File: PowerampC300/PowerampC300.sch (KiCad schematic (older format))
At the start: 101 parts, among them J1 Conn_01x02, J2 Conn_01x02, J3 Conn_01x02, J4 Conn_01x01, J5 Conn_01x01, J6 Conn_01x01, J7 Conn_01x01, J8 Conn_01x02, J9 Conn_Coaxial, Q1 BC546, Q10 MJE350, Q11 MJE340, Q12 MJE340, Q13 BC546, Q14 BC556, Q15 MJE340, Q16 MJE350, Q17 MJL3281A, Q18 MJL1302A, Q19 MJL3281A, Q2 BC546, Q20 MJL1302A, Q21 MJL3281A, Q22 MJL1302A, Q23 MJL3281A, Q24 MJL1302A, Q3 BC556, Q4 BC556, Q5 BC546, Q6 BC546, Q7 BC546, Q8 MPSA92, Q9 BC556

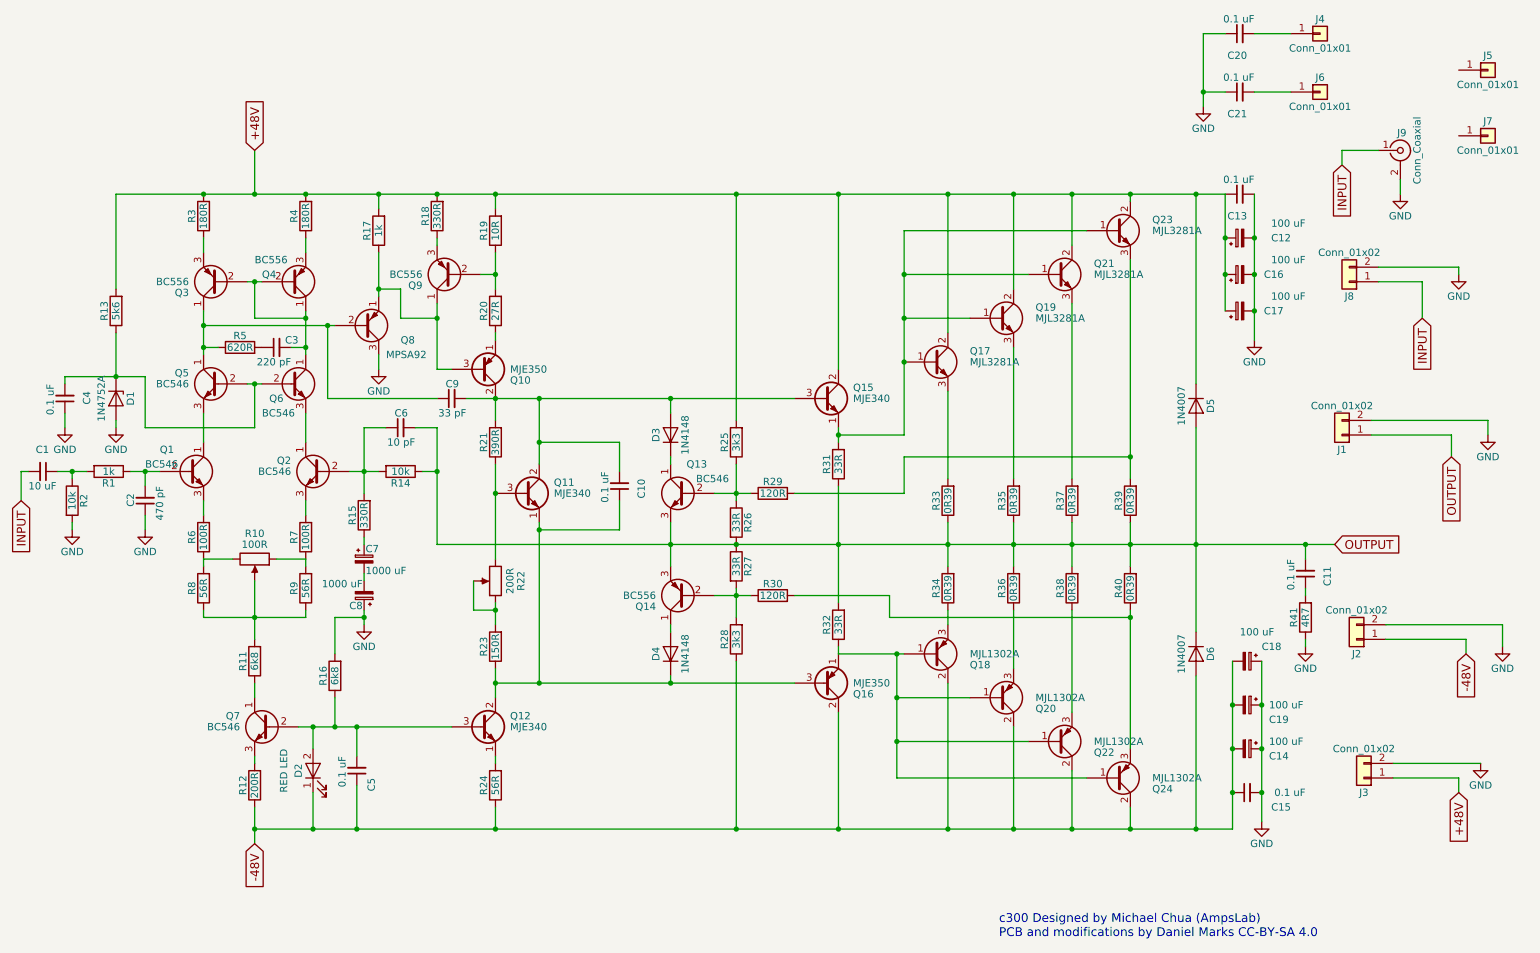
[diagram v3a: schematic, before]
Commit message: Changed softstart and Poweramp to TO-220 transistors
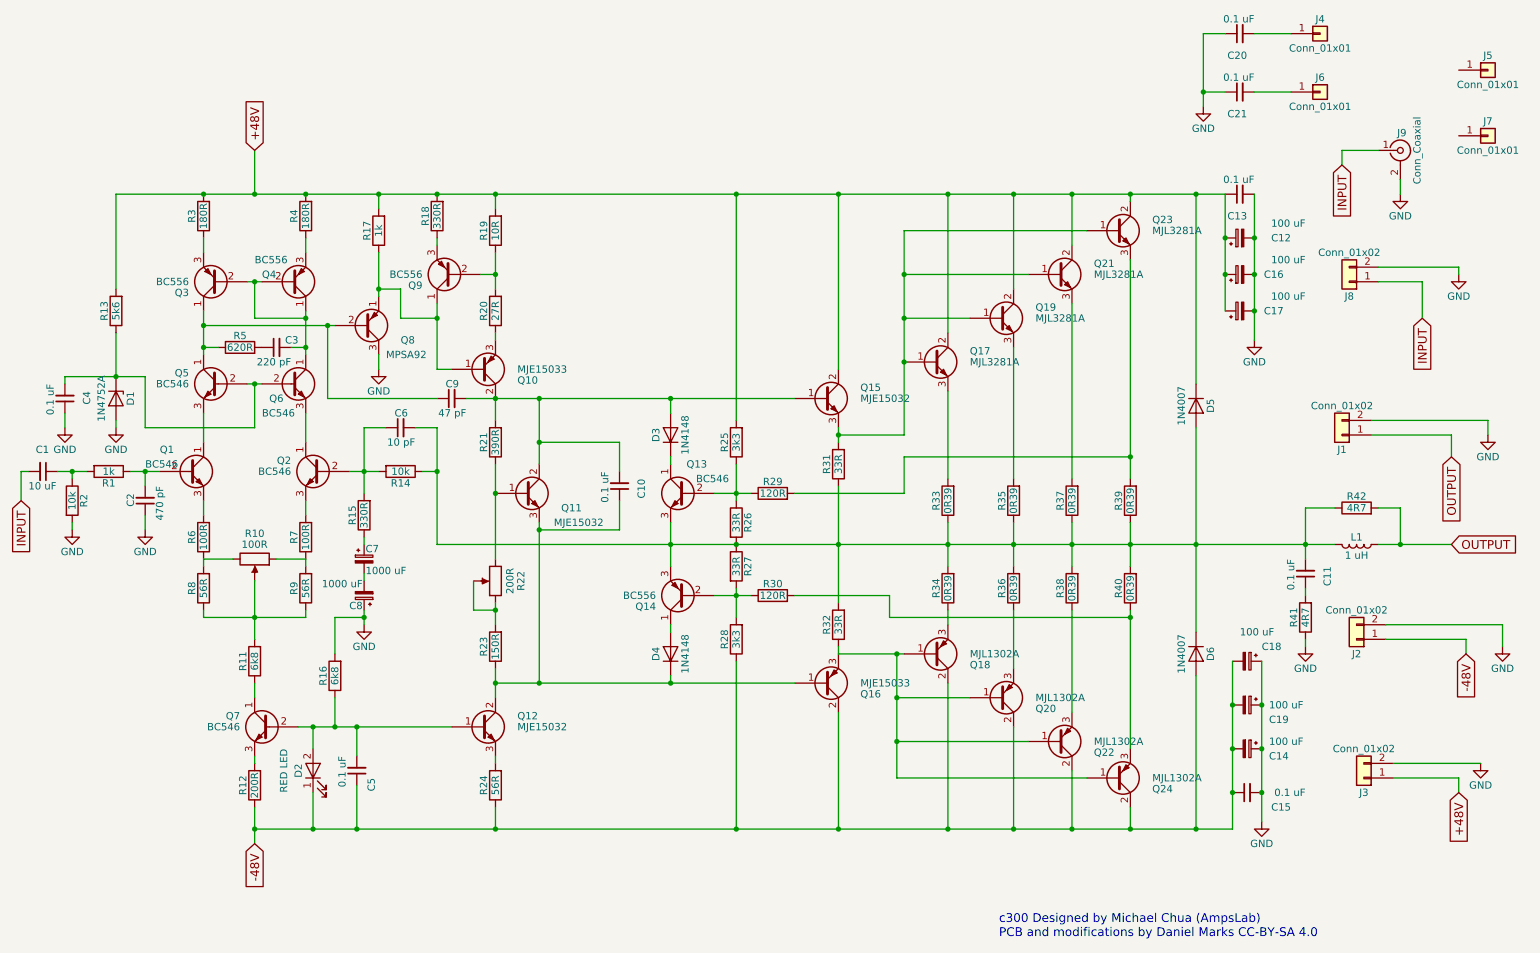
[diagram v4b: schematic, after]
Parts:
- removed Q10, Q16: MJE350, TO_SOT_Packages_THT:TO-126_Vertical, symbol BD140
- removed Q11, Q12, Q15: MJE340, TO_SOT_Packages_THT:TO-126_Vertical, symbol BD139
- added L1: 1 uH, Inductors_THT:L_Radial_D16.8mm_P11.43mm_Vishay_IHB-1, symbol L
- added Q10, Q16: MJE15033, TO_SOT_Packages_THT:TO-220-3_Vertical, symbol TIP42C
- added Q11, Q12, Q15: MJE15032, TO_SOT_Packages_THT:TO-220-3_Vertical, symbol TIP41C
- added R42: 4R7, Resistors_THT:R_Axial_DIN0411_L9.9mm_D3.6mm_P15.24mm_Horizontal, symbol R
- C9: value 33 pF -> 47 pF
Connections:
- net +48V: now also Q15.2 (C)
- net -48V: now also Q16.2 (C)
- net OUTPUT: now also L1.1, R42.2; no longer C11.2, C6.2, D5.2 (A), D6.1 (K), Q13.3 (E), Q14.3 (E), R14.1, R26.2, R27.1, R31.1, R32.2, R33.1, R34.2, R35.1, R36.2, R37.1, R38.2, R39.1, R40.2
- net at C5.2, D2.2 (A), Q7.2 (B)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: now also Q12.1 (B)
- net at R20.1: now also Q10.3 (E)
- net at C10.2, C9.2, D3.2 (A)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: now also Q10.2 (C), Q11.2 (C), Q15.1 (B)
- net at Q8.1 (E), Q9.1 (C), R17.1: now also Q10.1 (B)
- net at R24.2: now also Q12.3 (E)
- net at C10.1, D4.1 (K), R23.1: now also Q11.3 (E), Q12.2 (C), Q16.1 (B)
- net at R21.1, R22.3: now also Q11.1 (B)
- net at Q17.1 (B), Q19.1 (B), Q21.1 (B)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: now also Q15.3 (E)
- net at Q18.1 (B), Q20.1 (B), Q22.1 (B)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: now also Q16.3 (E)
- new net: C11.2, C6.2, D5.2 (A), D6.1 (K), L1.2, Q13.3 (E), Q14.3 (E), R14.1, R26.2, R27.1, R31.1, R32.2, R33.1, R34.2, R35.1, R36.2, R37.1, R38.2, R39.1, R40.2, R42.1
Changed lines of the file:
@@
-$EndComp
-$Comp
-L BD140 Q10
-U 1 1 5F3B4775
-P 3800 3000
-F 0 "Q10" H 4000 3075 50  0000 L CNN
-F 1 "MJE350" H 4000 3000 50  0000 L CNN
-F 2 "TO_SOT_Packages_THT:TO-126_Vertical" H 4000 2925 50  0001 L CIN
-F 3 "" H 3800 3000 50  0001 L CNN
-F 4 "C283403" H 3800 3000 60  0001 C CNN "LCSC"
-	1    3800 3000
-	1    0    0    1
 $EndComp
 $Comp
@@
 P 3600 3200
 F 0 "C9" V 3700 3150 50  0000 L CNN
-F 1 "33 pF" V 3500 3100 50  0000 L CNN
+F 1 "47 pF" V 3500 3100 50  0000 L CNN
 F 2 "Capacitors_THT:C_Disc_D5.0mm_W2.5mm_P5.00mm" H 3600 3200 50  0001 C CNN
 F 3 "" H 3600 3200 50  0001 C CNN
@@
 	1    3600 3200
 	0    -1   -1   0
-$EndComp
-$Comp
-L BD139 Q12
-U 1 1 5F3B79AE
-P 3800 5450
-F 0 "Q12" H 4000 5525 50  0000 L CNN
-F 1 "MJE340" H 4000 5450 50  0000 L CNN
-F 2 "TO_SOT_Packages_THT:TO-126_Vertical" H 4000 5375 50  0001 L CIN
-F 3 "" H 3800 5450 50  0001 L CNN
-F 4 "C283424" H 3800 5450 60  0001 C CNN "LCSC"
-F 5 "C142464" H 3800 5450 60  0001 C CNN "LCSC"
-	1    3800 5450
-	1    0    0    -1
 $EndComp
 $Comp
@@
 	1    3900 3500
 	-1   0    0    1
-$EndComp
-$Comp
-L BD139 Q11
-U 1 1 5F3B7E33
-P 4100 3850
-F 0 "Q11" H 4300 3925 50  0000 L CNN
-F 1 "MJE340" H 4300 3850 50  0000 L CNN
-F 2 "TO_SOT_Packages_THT:TO-126_Vertical" H 4300 3775 50  0001 L CIN
-F 3 "" H 4100 3850 50  0001 L CNN
-F 4 "C283424" H 4100 3850 60  0001 C CNN "LCSC"
-	1    4100 3850
-	1    0    0    -1
 $EndComp
 $Comp
@@
 $EndComp
 $Comp
-L BD139 Q15
-U 1 1 5F3BC2B3
-P 6150 3200
-F 0 "Q15" H 6350 3275 50  0000 L CNN
-F 1 "MJE340" H 6350 3200 50  0000 L CNN
-F 2 "TO_SOT_Packages_THT:TO-126_Vertical" H 6350 3125 50  0001 L CIN
-F 3 "" H 6150 3200 50  0001 L CNN
-F 4 "C283424" H 6150 3200 60  0001 C CNN "LCSC"
-	1    6150 3200
-	1    0    0    -1
-$EndComp
-$Comp
-L BD140 Q16
-U 1 1 5F3BC80D
-P 6150 5150
-F 0 "Q16" H 6350 5225 50  0000 L CNN
-F 1 "MJE350" H 6350 5150 50  0000 L CNN
-F 2 "TO_SOT_Packages_THT:TO-126_Vertical" H 6350 5075 50  0001 L CIN
-F 3 "" H 6150 5150 50  0001 L CNN
-F 4 "C283403" H 6150 5150 60  0001 C CNN "LCSC"
-	1    6150 5150
-	1    0    0    1
-$EndComp
-$Comp
 L R R31
 U 1 1 5F3BCB79
@@
 	1    0    0    -1
 $EndComp
-Text GLabel 9650 4200 2    60   Input ~ 0
+Text GLabel 10450 4200 2    60   Input ~ 0
 OUTPUT
 Text GLabel 650  3900 3    60   Input ~ 0
@@
 Connection ~ 8900 2350
 Wire Wire Line
-	9450 4300 9450 4200
+	9450 3950 9450 4300
 Connection ~ 9450 4200
 Connection ~ 9150 5600
@@
 Wire Wire Line
 	10800 4750 10800 4900
+$Comp
+L TIP41C Q12
+U 1 1 5F4FB282
+P 3800 5450
+F 0 "Q12" H 4050 5525 50  0000 L CNN
+F 1 "MJE15032" H 4050 5450 50  0000 L CNN
+F 2 "TO_SOT_Packages_THT:TO-220-3_Vertical" H 4050 5375 50  0001 L CIN
+F 3 "" H 3800 5450 50  0001 L CNN
+	1    3800 5450
+	1    0    0    -1
+$EndComp
+$Comp
+L TIP42C Q16
+U 1 1 5F4FB50E
+P 6150 5150
+F 0 "Q16" H 6400 5225 50  0000 L CNN
+F 1 "MJE15033" H 6400 5150 50  0000 L CNN
+F 2 "TO_SOT_Packages_THT:TO-220-3_Vertical" H 6400 5075 50  0001 L CIN
+F 3 "" H 6150 5150 50  0001 L CNN
+	1    6150 5150
+	1    0    0    1
+$EndComp
+$Comp
+L TIP41C Q11
+U 1 1 5F4FBF00
+P 4100 3850
+F 0 "Q11" H 4350 3750 50  0000 L CNN
+F 1 "MJE15032" H 4300 3650 50  0000 L CNN
+F 2 "TO_SOT_Packages_THT:TO-220-3_Vertical" H 4350 3775 50  0001 L CIN
+F 3 "" H 4100 3850 50  0001 L CNN
+	1    4100 3850
+	1    0    0    -1
+$EndComp
+$Comp
+L TIP41C Q15
+U 1 1 5F4FC974
+P 6150 3200
+F 0 "Q15" H 6400 3275 50  0000 L CNN
+F 1 "MJE15032" H 6400 3200 50  0000 L CNN
+F 2 "TO_SOT_Packages_THT:TO-220-3_Vertical" H 6400 3125 50  0001 L CIN
+F 3 "" H 6150 3200 50  0001 L CNN
+	1    6150 3200
+	1    0    0    -1
+$EndComp
+$Comp
+L TIP42C Q10
+U 1 1 5F500035
+P 3800 3000
+F 0 "Q10" H 4050 3075 50  0000 L CNN
+F 1 "MJE15033" H 4050 3000 50  0000 L CNN
+F 2 "TO_SOT_Packages_THT:TO-220-3_Vertical" H 4050 2925 50  0001 L CIN
+F 3 "" H 3800 3000 50  0001 L CNN
+	1    3800 3000
+	1    0    0    1
+$EndComp
+$Comp
+L L L1
+U 1 1 5F55AD15
+P 9800 4200
+F 0 "L1" V 9750 4200 50  0000 C CNN
+F 1 "1 uH" V 9875 4200 50  0000 C CNN
+F 2 "Inductors_THT:L_Radial_D16.8mm_P11.43mm_Vishay_IHB-1" H 9800 4200 50  0001 C CNN
+F 3 "" H 9800 4200 50  0001 C CNN
+	1    9800 4200
+	0    1    1    0
+$EndComp
+$Comp
+L R R42
+U 1 1 5F55B21A
+P 9800 3950
+F 0 "R42" V 9880 3950 50  0000 C CNN
+F 1 "4R7" V 9800 3950 50  0000 C CNN
+F 2 "Resistors_THT:R_Axial_DIN0411_L9.9mm_D3.6mm_P15.24mm_Horizontal" V 9730 3950 50  0001 C CNN
+F 3 "" H 9800 3950 50  0001 C CNN
+F 4 "C138189" V 9800 3950 60  0001 C CNN "LCSC"
+	1    9800 3950
+	0    -1   -1   0
+$EndComp
+Wire Wire Line
+	9650 3950 9450 3950
+Wire Wire Line
+	9950 3950 10100 3950
+Wire Wire Line
+	10100 3950 10100 4200
+Wire Wire Line
+	9950 4200 10450 4200
+Connection ~ 10100 4200
 $EndSCHEMATC

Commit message: Changed to 2N5551/2N5401 from BC546C/BC556C transistors
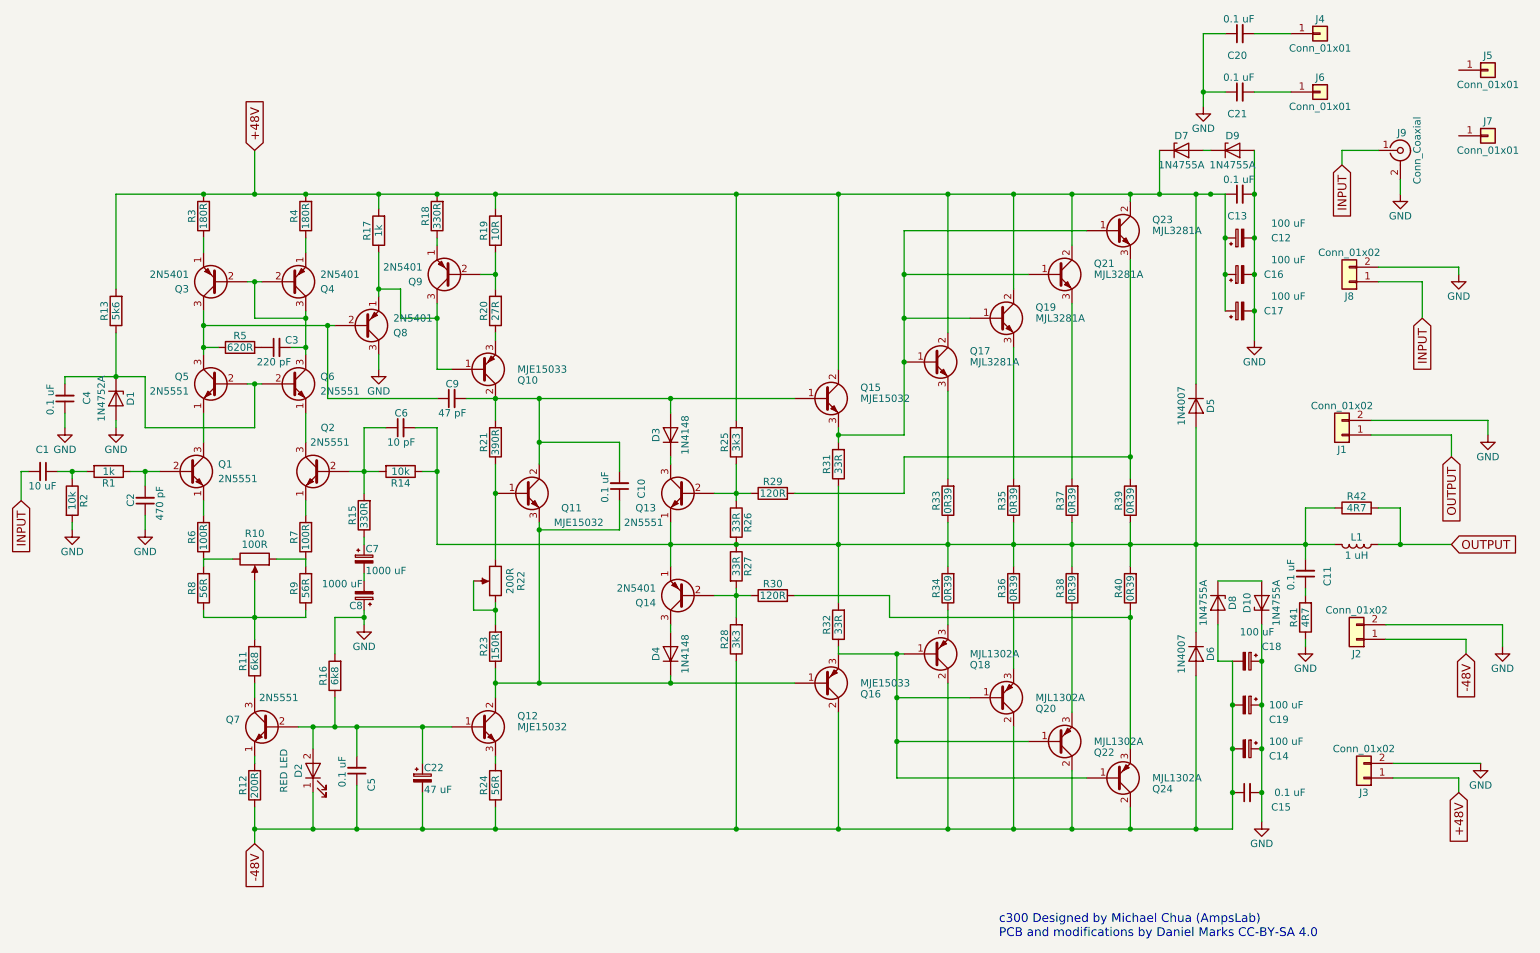
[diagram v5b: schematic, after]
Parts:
- removed Q1, Q13, Q2, Q5, Q6, Q7: BC546, TO_SOT_Packages_THT:TO-92_Molded_Narrow, symbol BC546
- removed Q14, Q3, Q4, Q9: BC556, TO_SOT_Packages_THT:TO-92_Molded_Narrow, symbol BC556
- removed Q8: MPSA92, TO_SOT_Packages_THT:TO-92_Molded_Narrow, symbol 2N3906
- added C22: 47 uF, Capacitors_THT:CP_Radial_D5.0mm_P2.50mm, symbol CP_Small
- added D10, D7, D8, D9: 1N4755A, Diodes_THT:D_DO-41_SOD81_P7.62mm_Horizontal, symbol D_Zener
- added Q1, Q13, Q2, Q5, Q6, Q7: 2N5551, TO_SOT_Packages_THT:TO-92_Inline_Wide, symbol Q_NPN_EBC
- added Q14, Q3, Q4, Q8, Q9: 2N5401, TO_SOT_Packages_THT:TO-92_Inline_Wide, symbol Q_PNP_EBC
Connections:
- net +48V: now also D7.1 (K)
- net -48V: now also C22.2, D8.2 (A)
- net GND: now also D10.1 (K), D9.2 (A), Q8.3 (C)
- net at C2.2, R1.1: now also Q1.2 (B)
- net at R6.2: now also Q1.1 (E)
- net at C6.1, R14.2, R15.2: now also Q2.2 (B)
- net at R7.2: now also Q2.1 (E)
- net at R11.1: now also Q7.3 (C)
- net at R12.2: now also Q7.1 (E)
- net at C5.2, D2.2 (A), Q12.1 (B)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: now also C22.1, Q7.2 (B)
- net at C9.1, R5.1: now also Q3.3 (C), Q5.3 (C), Q8.2 (B)
- net at C4.2, D1.1 (K), R13.1: now also Q5.2 (B), Q6.2 (B)
- net at C3.2: now also Q3.2 (B), Q4.2 (B), Q4.3 (C), Q6.3 (C)
- net at R4.1: now also Q4.1 (E)
- net at R3.1: now also Q3.1 (E)
- net at C11.2, C6.2, D5.2 (A)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: now also Q13.1 (E), Q14.1 (E)
- net at Q10.1 (B), R17.1: now also Q8.1 (E), Q9.3 (C)
- net at R19.1, R20.2: now also Q9.2 (B)
- net at R18.1: now also Q9.1 (E)
- net at D3.1 (K): now also Q13.3 (C)
- net at R25.1, R26.1, R29.1: now also Q13.2 (B)
- net at D4.2 (A): now also Q14.3 (C)
- net at R27.2, R28.2, R30.1: now also Q14.2 (B)
- new net: Q1.3 (C), Q5.1 (E)
- new net: Q2.3 (C), Q6.1 (E)
- new net: D7.2 (A), D9.1 (K)
- new net: D10.2 (A), D8.1 (K)
